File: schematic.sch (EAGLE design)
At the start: 40 parts, among them CN1 1X4-BIG, CN2 1X4-BIG, IC3 78TO220, IC4 78TO220

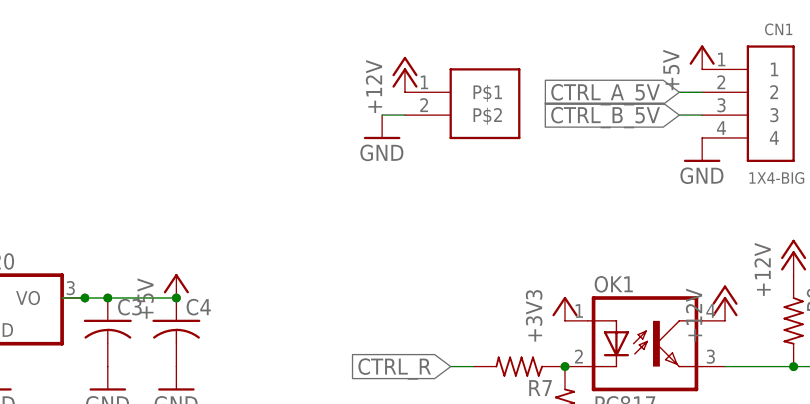
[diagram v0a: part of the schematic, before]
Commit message: Added board alongation for J4 connector
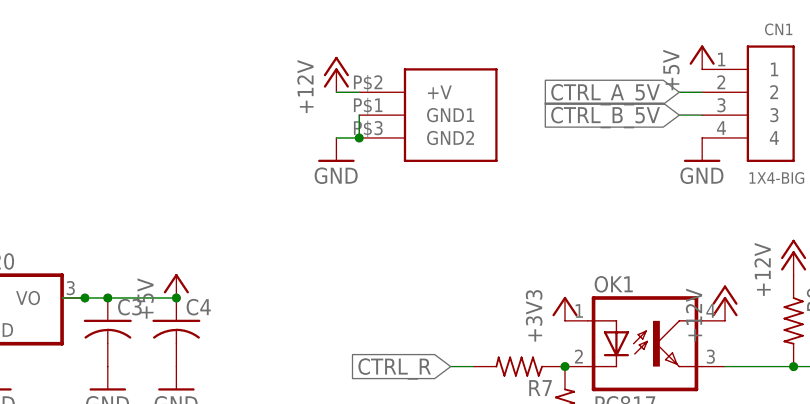
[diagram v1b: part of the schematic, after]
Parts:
- U$2: value HEADER-2X1 -> J4-2.2X5.1; device z-lib:HEADER-2X1 -> z-lib:J4-2.2X5.1
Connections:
- net +12V: now also U$2.+V; no longer U$2.P$1
- net GND: now also U$2.GND1, U$2.GND2; no longer U$2.P$2
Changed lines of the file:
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@@
 <part name="U$1" library="z-lib" deviceset="ESP8266" device=""/>
 <part name="+3V11" library="supply1" library_urn="urn:adsk.eagle:library:371" deviceset="+3V3" device=""/>
-<part name="U$2" library="z-lib" deviceset="HEADER-2X1" device=""/>
 <part name="IC3" library="adafruit" deviceset="78*" device="TO220"/>
 <part name="IC4" library="adafruit" deviceset="78*" device="TO220"/>
+<part name="U$2" library="z-lib" deviceset="J4-2.2X5.1" device=""/>
 </parts>
 <sheets>
@@
 <instance part="CN1" gate="G$1" x="106.68" y="121.92"/>
 <instance part="CN2" gate="G$1" x="132.08" y="121.92"/>
-<instance part="P+4" gate="1" x="68.58" y="124.46"/>
-<instance part="GND10" gate="1" x="66.04" y="116.84"/>
+<instance part="P+4" gate="1" x="60.96" y="124.46"/>
+<instance part="GND10" gate="1" x="60.96" y="114.3"/>
 <instance part="GND11" gate="1" x="101.6" y="114.3"/>
 <instance part="GND12" gate="1" x="127" y="114.3"/>
@@
 <instance part="U$1" gate="G$1" x="15.24" y="40.64"/>
 <instance part="+3V11" gate="G$1" x="-5.08" y="12.7"/>
-<instance part="U$2" gate="G$1" x="73.66" y="121.92"/>
 <instance part="IC3" gate="A1" x="22.86" y="99.06"/>
 <instance part="IC4" gate="A1" x="22.86" y="81.28"/>
+<instance part="U$2" gate="G$1" x="68.58" y="119.38"/>
 </instances>
 <busses>
@@
 </segment>
 <segment>
-<pinref part="GND10" gate="1" pin="GND"/>
-<pinref part="U$2" gate="G$1" pin="P$2"/>
-<wire x1="66.04" y1="119.38" x2="68.58" y2="119.38" width="0.1524" layer="91"/>
-</segment>
-<segment>
 <pinref part="R1" gate="G$1" pin="2"/>
 <pinref part="GND9" gate="1" pin="GND"/>
 <wire x1="30.48" y1="58.42" x2="33.02" y2="58.42" width="0.1524" layer="91"/>
+</segment>
+<segment>
+<pinref part="U$2" gate="G$1" pin="GND2"/>
+<pinref part="GND10" gate="1" pin="GND"/>
+<wire x1="63.5" y1="116.84" x2="60.96" y2="116.84" width="0.1524" layer="91"/>
+<pinref part="U$2" gate="G$1" pin="GND1"/>
+<wire x1="63.5" y1="119.38" x2="63.5" y2="116.84" width="0.1524" layer="91"/>
+<junction x="63.5" y="116.84"/>
 </segment>
 </net>
@@
 <segment>
 <pinref part="P+4" gate="1" pin="+12V"/>
-<pinref part="U$2" gate="G$1" pin="P$1"/>
-</segment>
-</net>
+<pinref part="U$2" gate="G$1" pin="+V"/>
+<wire x1="60.96" y1="121.92" x2="63.5" y2="121.92" width="0.1524" layer="91"/>
+</segment>
+</net>
